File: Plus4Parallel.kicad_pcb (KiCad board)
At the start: 2 copper layers, 69 x 18.7 mm, 3 parts, among them CN1 PLUS4_USERPORT, J1 DB25_Female_MountingHoles

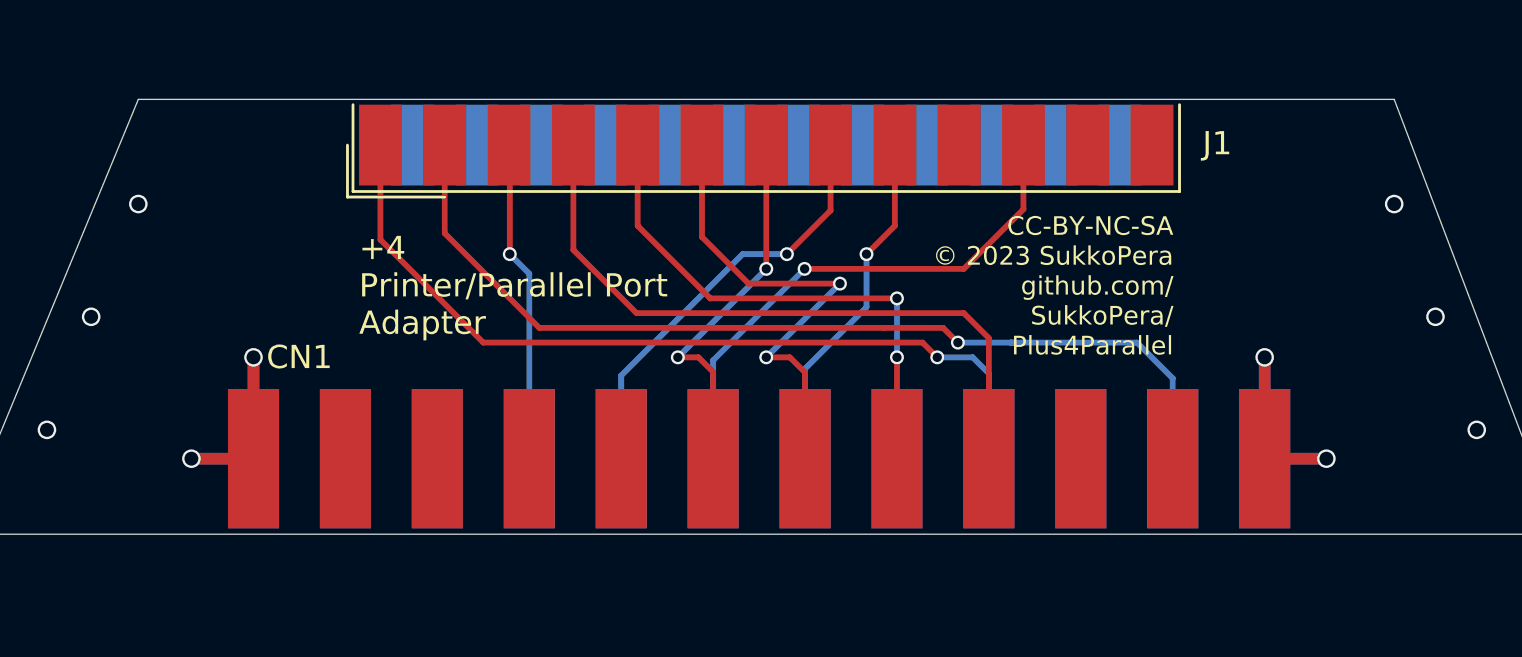
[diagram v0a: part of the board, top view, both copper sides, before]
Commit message: Add power jumper Inspired by Amiga
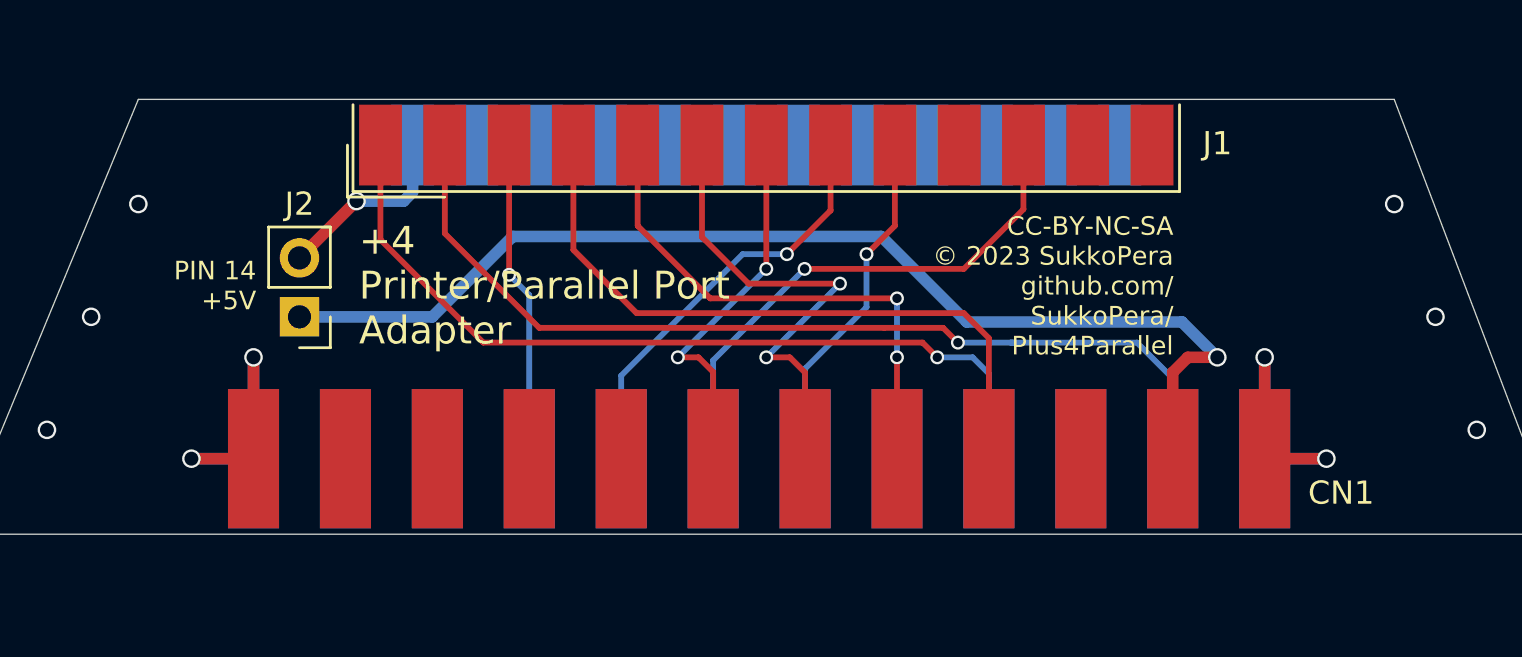
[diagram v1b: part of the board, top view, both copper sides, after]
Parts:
- added J2: JMP_POWER, Connector_PinHeader_2.54mm:PinHeader_1x02_P2.54mm_Vertical, F.Cu at (167.2, 81.7)
- moved V0 35.6 mm to (204.9, 80.4)
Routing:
- net +5V: track 0.00 -> 49.0 mm, vias 0 -> 1
- net Net-(J1-Pad14): track 0.00 -> 8.07 mm, vias 0 -> 1
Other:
- board text added: "PIN 14 +5V"

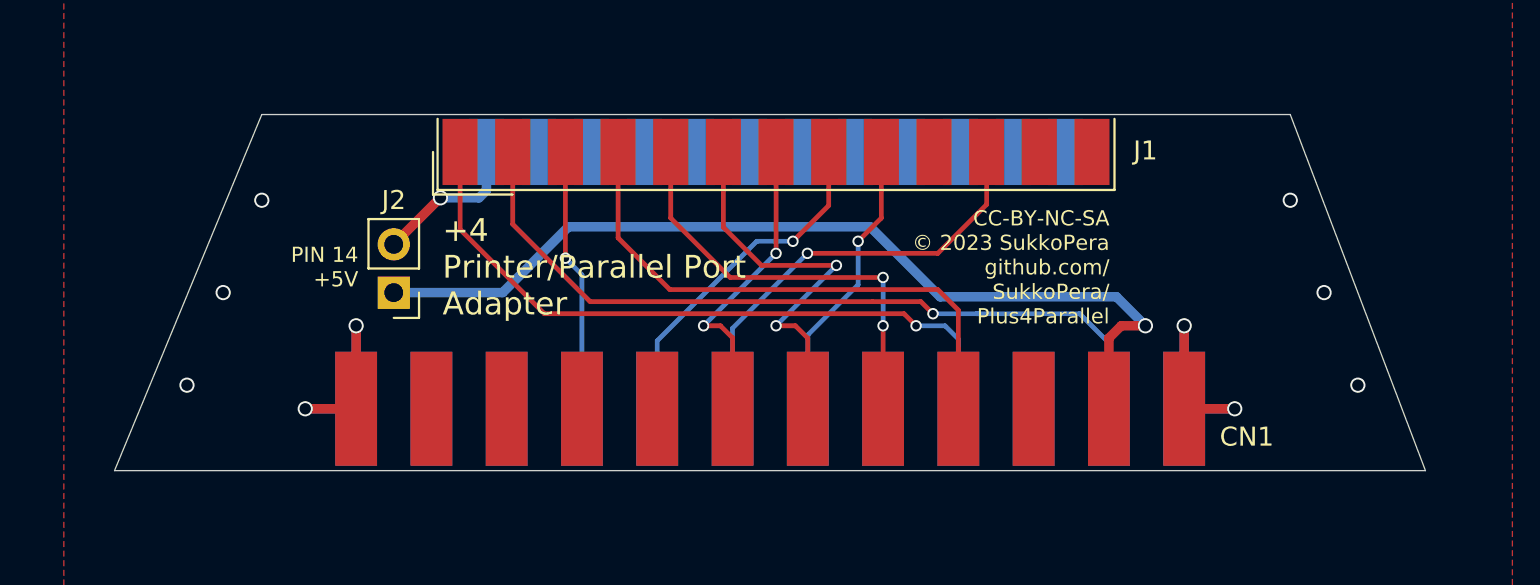
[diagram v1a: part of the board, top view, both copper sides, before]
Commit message: Work on simmetry Note that DB-25 footprint is still not centered, don't know why!
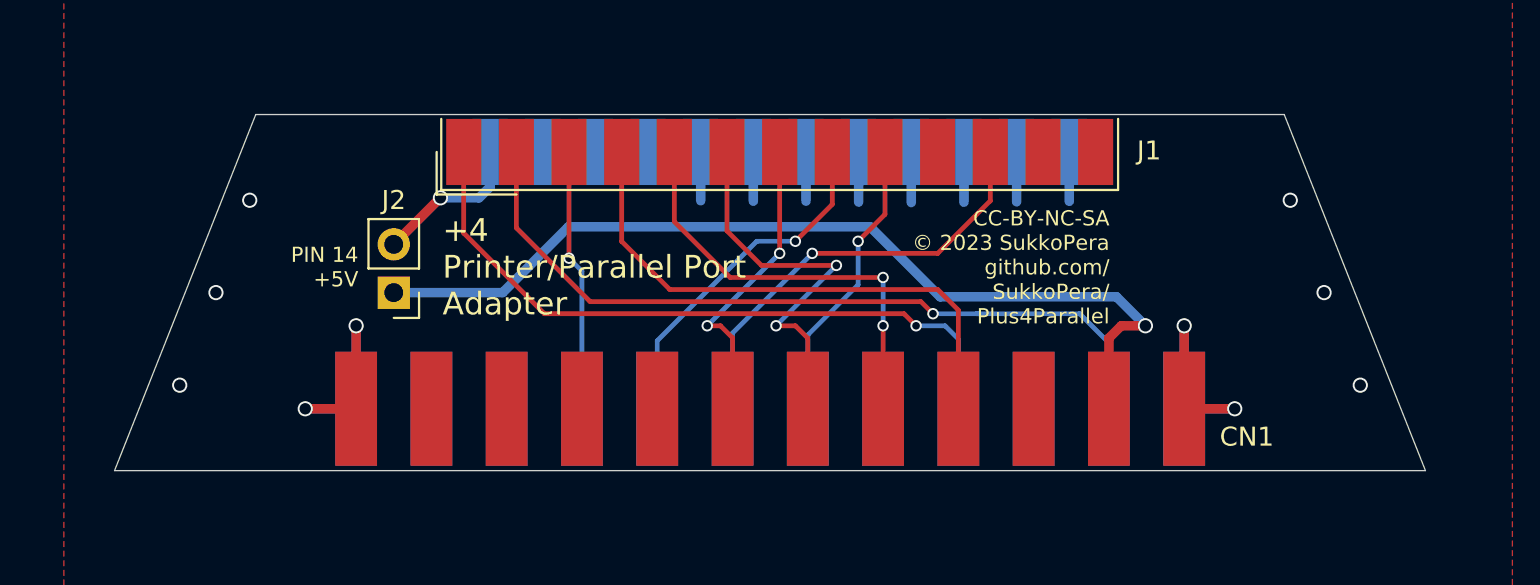
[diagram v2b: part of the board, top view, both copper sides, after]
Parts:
- moved J1 0.19 mm to (187.5, 74.3)
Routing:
- net GND: track 28.0 -> 48.9 mm
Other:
- outline, holes or cut-outs redrawn

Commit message: +4 -> Plus/4
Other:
- board text added: "Plus/4 Printer/Parallel Port Adapter"
- board text removed: "+4 Printer/Parallel Port Adapter"
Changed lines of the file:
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@@
     (31 B.Cu signal)
     (36 B.SilkS user)
-    (37 F.SilkS user hide)
+    (37 F.SilkS user)
     (38 B.Mask user)
     (39 F.Mask user)
@@
     (effects (font (size 0.8 0.8) (thickness 0.12)) (justify right))
   )
-  (gr_text "+4\nPrinter/Parallel Port\nAdapter" (at 169.781667 80.3525) (layer F.SilkS)
+  (gr_text "Plus/4\nPrinter/Parallel Port\nAdapter" (at 169.781667 80.3525) (layer F.SilkS)
     (effects (font (size 1.2 1.2) (thickness 0.15)) (justify left))
   )
